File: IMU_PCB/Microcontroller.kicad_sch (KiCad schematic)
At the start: 14 parts, among them J4 Conn_01x02_Pin, U10 Thermal Resistor, U2 ESP32-DEVKIT-C, U6 TJA1050T/CM,118, U7 SparkFun: ISM330DHCX, MMC5983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, U8 SDIO Card Breakout Board, U9 AM2302

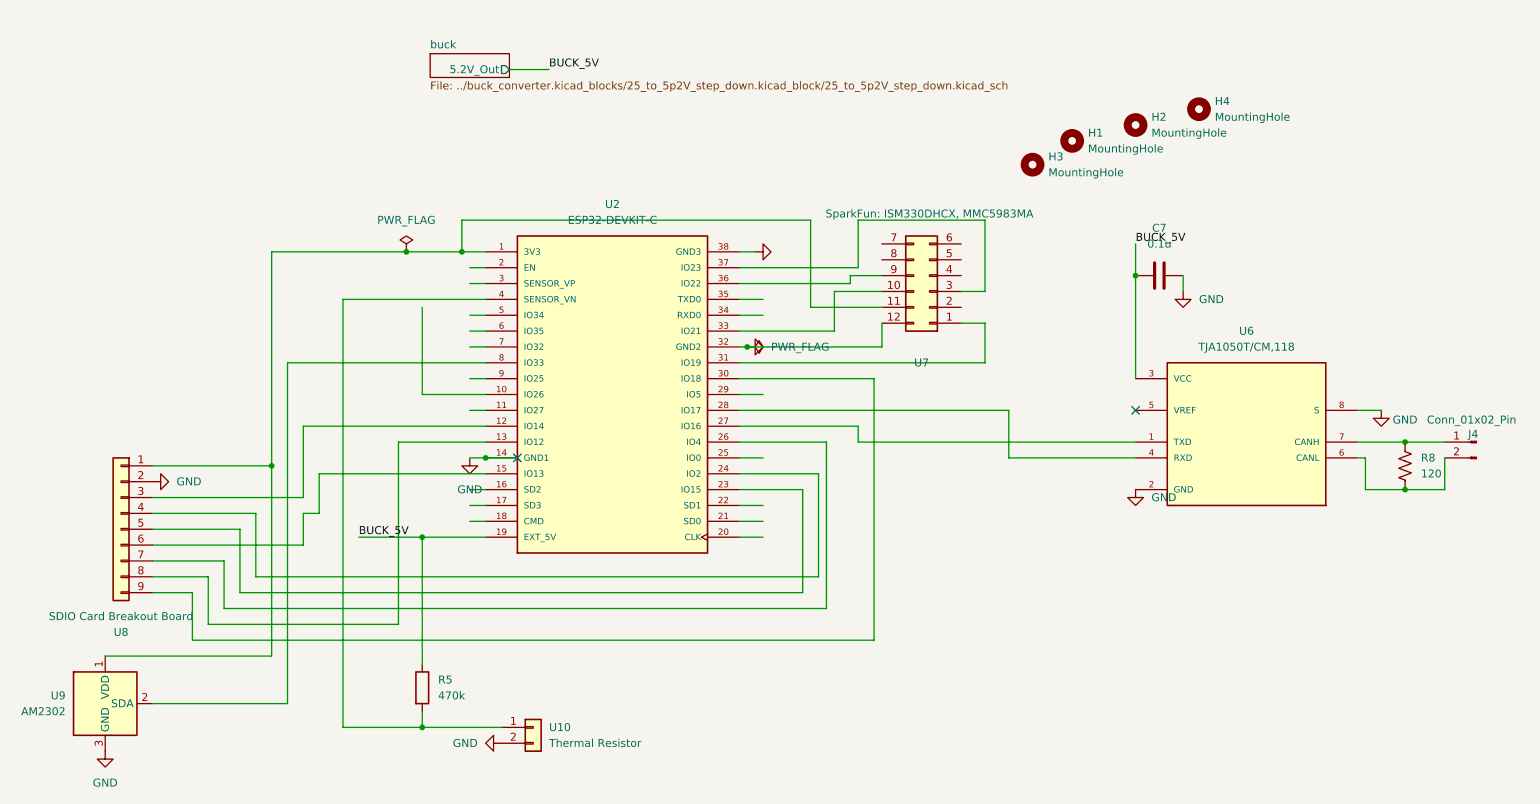
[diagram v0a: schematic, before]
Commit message: sry forgot to push, waiting on PCB shipping atm. Notes: split power distribution into two boards, one for the main 25V distribution, and another for 12V stuff. Also updated CAN transciever. the previous one was a 5V logic one (same logic as its power), and would have fried our ESPs data pins
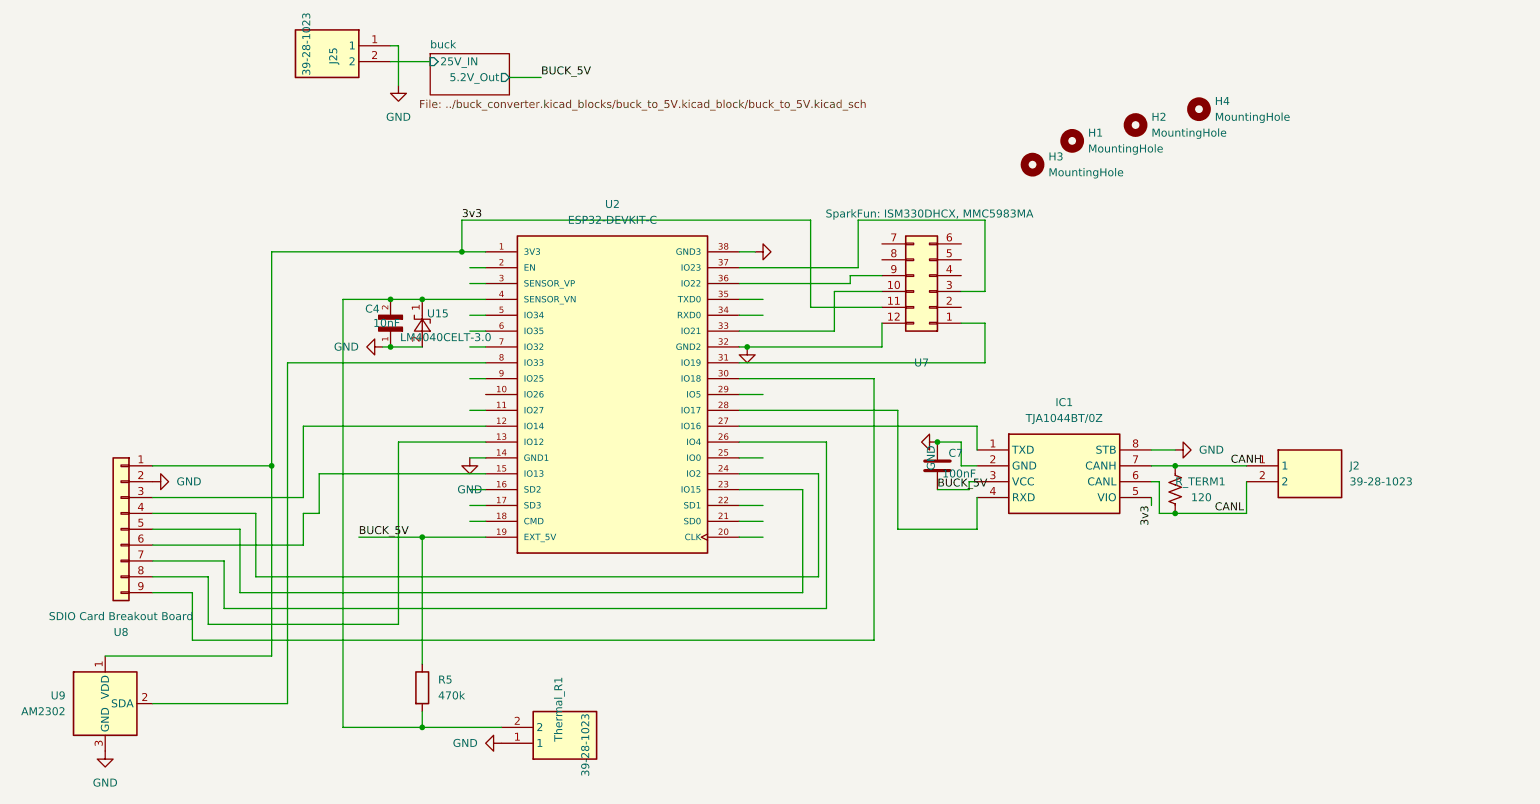
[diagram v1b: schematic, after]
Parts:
- removed J4: Conn_01x02_Pin, PROVE-footprints:TE_1877285-2, symbol Connector:Conn_01x02_Pin
- removed R8: 120, Resistor_SMD:R_1206_3216Metric_Pad1.30x1.75mm_HandSolder, symbol PROVE:RMCF1206JT120R
- removed U10: Thermal Resistor, PROVE-footprints:TE_1877285-2, symbol Connector_Generic:Conn_01x02
- removed U6: TJA1050T/CM,118, Package_SO:SOIC-8_3.9x4.9mm_P1.27mm, symbol PROVE:TJA1050T/CM,118
- added C4: 10nF, Capacitor_SMD:C_0805_2012Metric_Pad1.18x1.45mm_HandSolder, symbol C0805C122J5GACTU:C0805C122J5GACTU
- added IC1: TJA1044BT/0Z, PROVE-footprints:SOIC127P600X175-8N, symbol PROVE_Symbols:TJA1044BT_0Z
- added J2, J25, Thermal_R1: 39-28-1023, PROVE-footprints:39-28-1023, symbol PROVE_Symbols:39-28-1023
- added R_TERM1: 120, Resistor_SMD:R_0805_2012Metric_Pad1.20x1.40mm_HandSolder, symbol PROVE:RMCF1206JT120R
- added U15: LM4040CELT-3.0, Package_TO_SOT_SMD:SOT-23, symbol Reference_Voltage:LM4040DBZ-3
- C7: value 0.1u -> 100nF; footprint Capacitor_SMD:C_1206_3216Metric_Pad1.33x1.80mm_HandSolder -> Capacitor_SMD:C_0805_2012Metric_Pad1.18x1.45mm_HandSolder; Purchase Link (none) -> https://www.mouser.com/en/ProductDetail/KEMET/C0805X104K1RA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; Specs (none) -> 100 nF, 100 V, X7R, ±10%
- R5: Purchase Link (none) -> https://www.mouser.com/en/ProductDetail/KOA-Speer/SG73P2ATT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
- U7: Purchase Link (none) -> https://www.sparkfun.com/sparkfun-9dof-imu-breakout-ism330d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
- U9: footprint Sensor:ASAIR_AM2302_P2.54mm_Vertical -> PROVE-footprints:ASAIR_AM2302_P2.54mm_Vertical; Purchase Link (none) -> https://www.amazon.com/dp/B0795F19W6?ref_=ppx_hzsearch_conn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
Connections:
- net BUCK_5V: now also C7.1, IC1.3 (VCC); no longer C7.2
- net GND: now also C7.2, C4.1, IC1.2 (GND), IC1.8 (STB), J25.1, Thermal_R1.1, U15.2 (A); no longer C7.1
- net 3v3: now reaches U2.1 (3V3), U7.11 (Pin_11), U8.1 (Pin_1), U9.1 (VDD)
- net 3v3: now also IC1.5 (VIO)
- net at R5.2, U2.4 (SENSOR_VN): now also C4.2, Thermal_R1.2, U15.1 (K)
- net at U2.27 (IO16): now also IC1.1 (TXD)
- net at U2.28 (IO17): now also IC1.4 (RXD)
- new net CANH: IC1.7 (CANH), J2.1, R_TERM1.1
- new net CANL: IC1.6 (CANL), J2.2, R_TERM1.2
- new net buck/25V_IN: J25.2
- no-connect marks 2 -> 0
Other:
- sheet buck: file ../buck_converter.kicad_blocks/25_to_5p2V_step_down.kicad_block/25_to_5p2V_step_down.kicad_sch -> ../buck_converter.kicad_blocks/buck_to_5V.kicad_block/buck_to_5V.kicad_sch
- sheet buck ports: added 25V_IN; removed none
